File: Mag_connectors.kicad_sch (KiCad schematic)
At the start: 4 parts

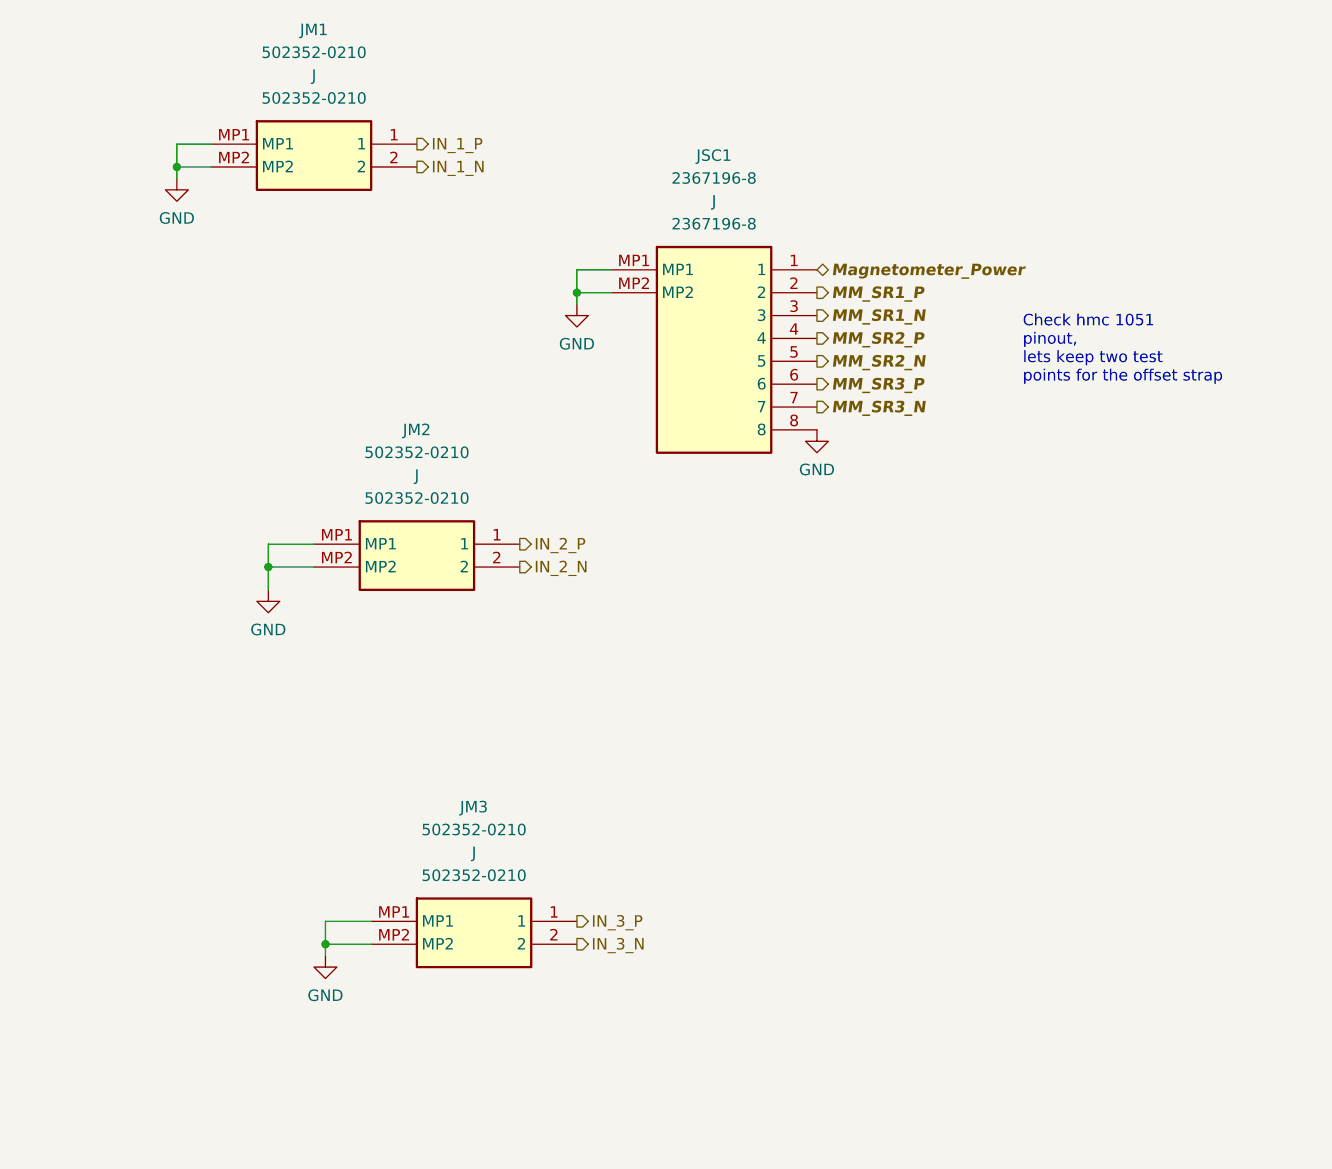
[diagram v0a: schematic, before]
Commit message: magnetometer connector corrected
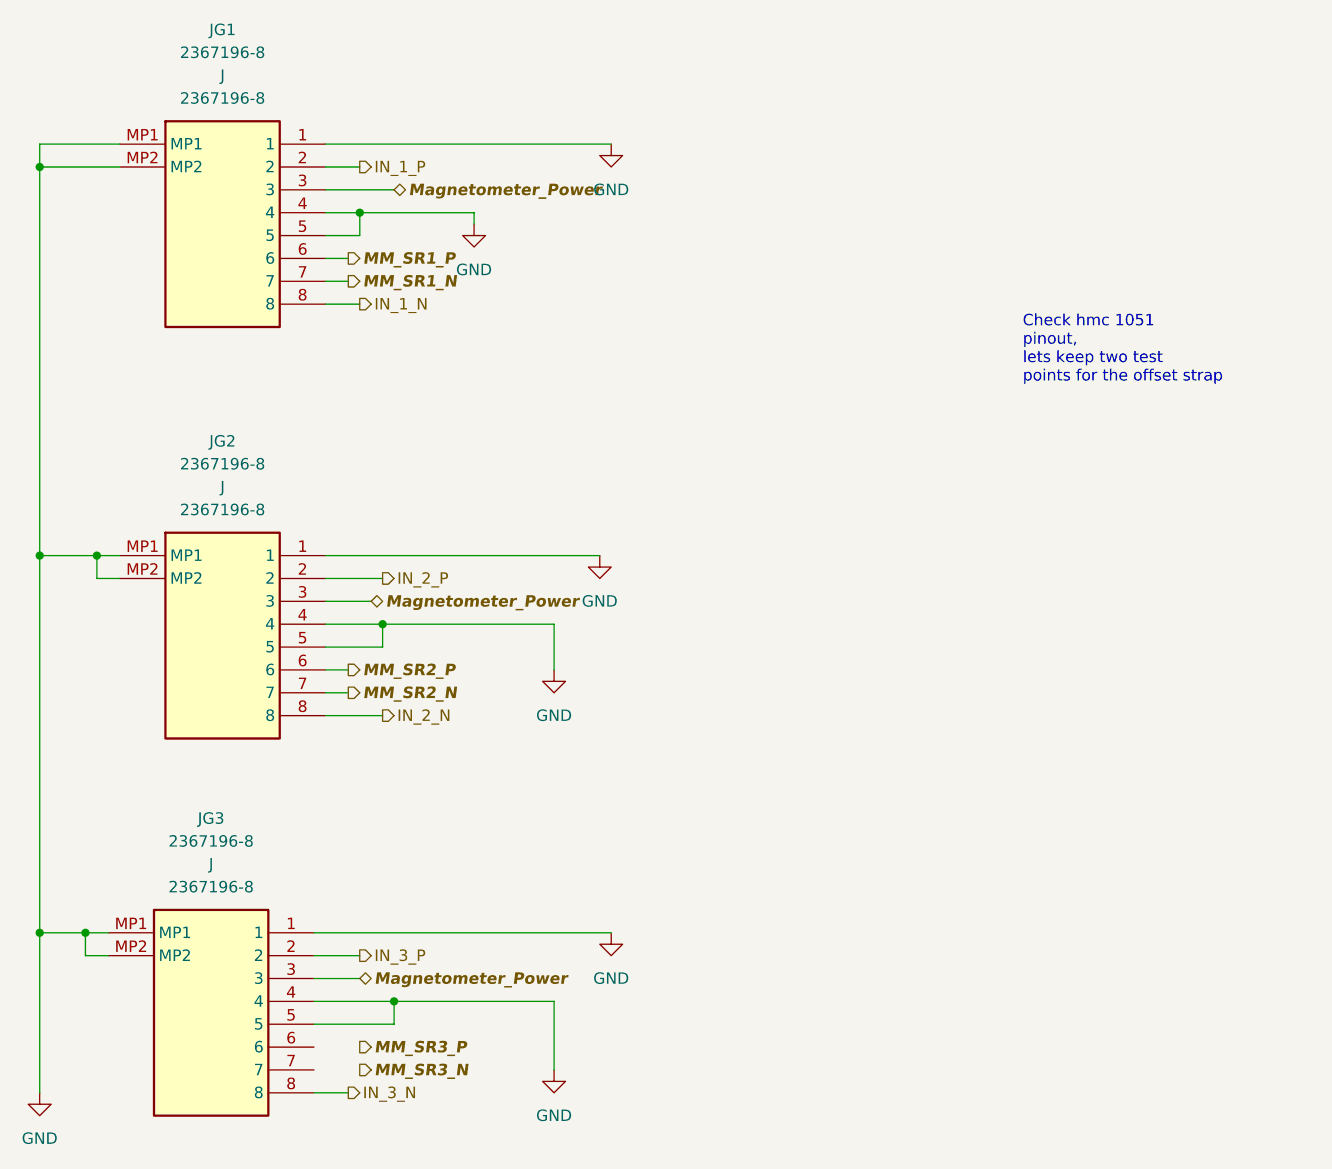
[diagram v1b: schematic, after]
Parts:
- removed JM1, JM2, JM3: 502352-0210, symbol 502352-0210:502352-0210
- removed JSC1: 2367196-8, symbol 2367196-8:2367196-8
- added JG1, JG2, JG3: 2367196-8, symbol 2367196-8:2367196-8
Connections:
- net GND: now also JG1.1, JG1.4, JG1.5, JG1.MP1, JG1.MP2, JG2.1, JG2.4, JG2.5, JG2.MP1, JG2.MP2, JG3.1, JG3.4, JG3.5, JG3.MP1, JG3.MP2
- net IN_1_N: now also JG1.8
- net IN_1_P: now also JG1.2
- net IN_2_N: now also JG2.8
- net IN_2_P: now also JG2.2
- net IN_3_N: now also JG3.8
- net IN_3_P: now also JG3.2
- net MM_SR1_N: now also JG1.7
- net MM_SR1_P: now also JG1.6
- net MM_SR2_N: now also JG2.7
- net MM_SR2_P: now also JG2.6
- net Magnetometer_Power: now also JG1.3, JG2.3, JG3.3

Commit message: ERC cleared in magnetometer connectors sheet
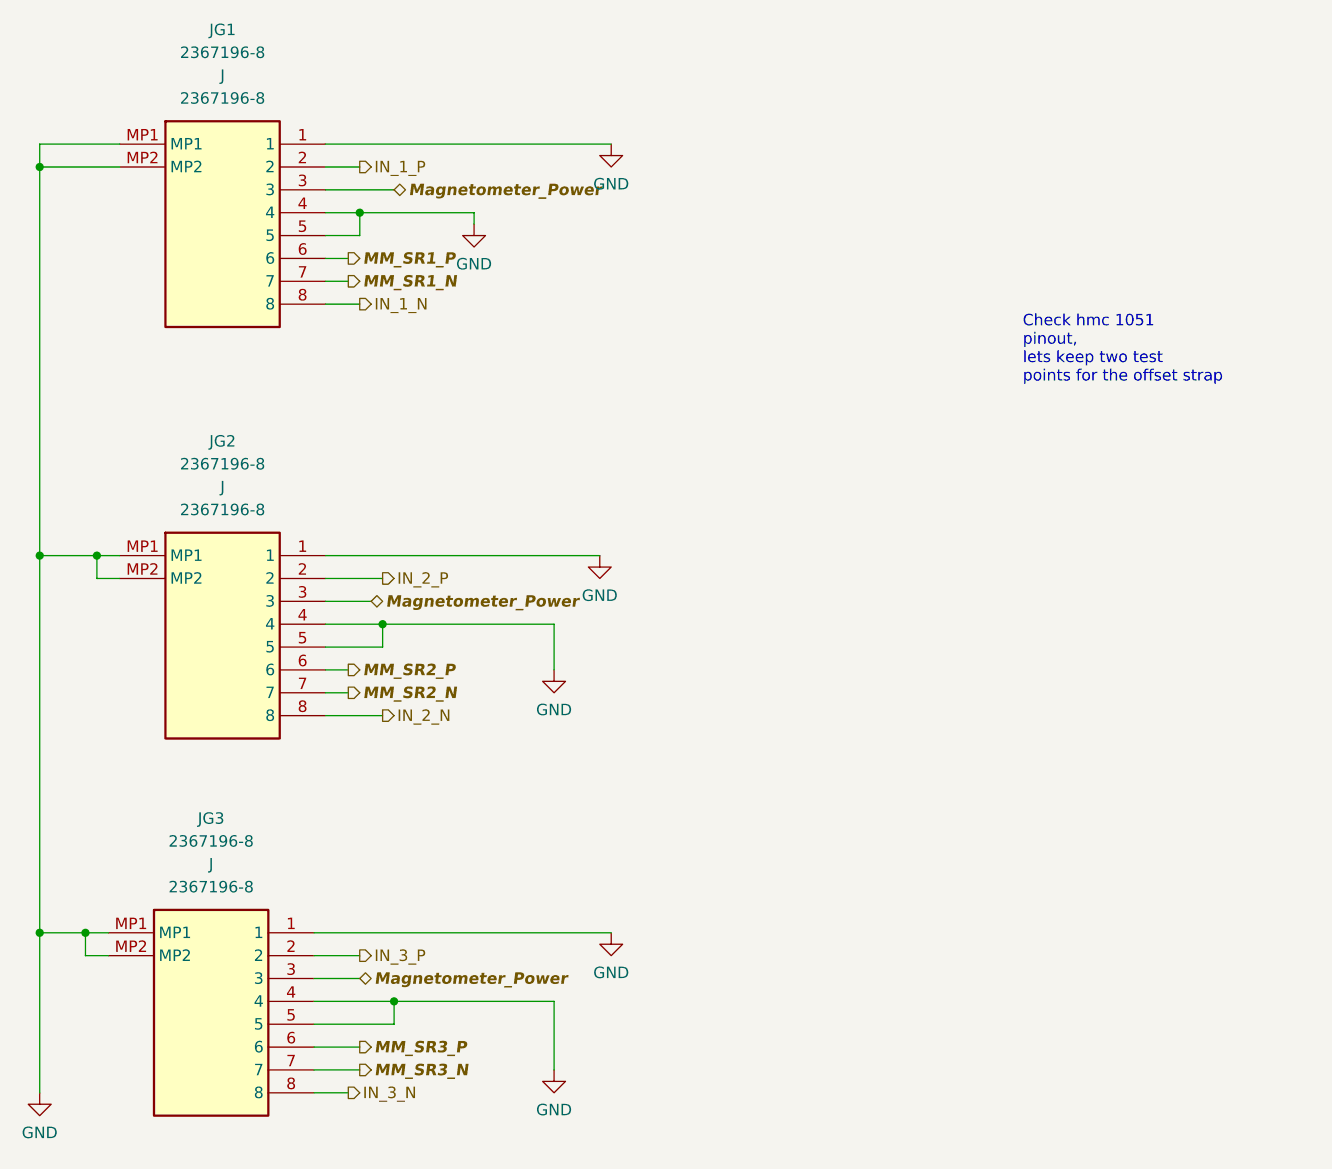
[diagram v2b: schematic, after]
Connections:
- net MM_SR3_N: now also JG3.7
- net MM_SR3_P: now also JG3.6
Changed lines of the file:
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@@
+    (stroke (width 0) (type default) (color 0 0 0 0))
+  )
+  (wire (pts (xy 76.2 149.86) (xy 81.28 149.86))
     (stroke (width 0) (type default) (color 0 0 0 0))
   )
   (wire (pts (xy 102.87 102.87) (xy 102.87 107.95))
+    (stroke (width 0) (type default) (color 0 0 0 0))
+  )
+  (wire (pts (xy 76.2 152.4) (xy 81.28 152.4))
     (stroke (width 0) (type default) (color 0 0 0 0))
   )
@@
   (hierarchical_label "Magnetometer_Power" (shape bidirectional) (at 82.55 100.33 0)
     (effects (font (size 1.27 1.27) bold italic) (justify left))
-  )
-  (symbol (lib_id "power:GND") (at 102.87 152.4 0) (unit 1)
-    (in_bom yes) (on_board yes) (fields_autoplaced)
-    (property "Reference" "#PWR?" (id 0) (at 102.87 158.75 0)
-      (effects (font (size 1.27 1.27)) hide)
-    )
-    (property "Value" "GND" (id 1) (at 102.87 157.48 0))
-    (property "Footprint" "" (id 2) (at 102.87 152.4 0)
-      (effects (font (size 1.27 1.27)) hide)
-    )
-    (property "Datasheet" "" (id 3) (at 102.87 152.4 0)
-      (effects (font (size 1.27 1.27)) hide)
-    )
-    (pin "1")
-  )
-  (symbol (lib_id "power:GND") (at 109.22 49.53 0) (unit 1)
-    (in_bom yes) (on_board yes) (fields_autoplaced)
-    (property "Reference" "#PWR?" (id 0) (at 109.22 55.88 0)
-      (effects (font (size 1.27 1.27)) hide)
-    )
-    (property "Value" "GND" (id 1) (at 109.22 54.61 0))
-    (property "Footprint" "" (id 2) (at 109.22 49.53 0)
-      (effects (font (size 1.27 1.27)) hide)
-    )
-    (property "Datasheet" "" (id 3) (at 109.22 49.53 0)
-      (effects (font (size 1.27 1.27)) hide)
-    )
-    (pin "1")
   )
   (symbol (lib_id "2367196-8:2367196-8") (at 54.61 95.25 0) (unit 1)
@@
     (pin "MP2")
   )
-  (symbol (lib_id "power:GND") (at 102.87 107.95 0) (unit 1)
-    (in_bom yes) (on_board yes) (fields_autoplaced)
-    (property "Reference" "#PWR?" (id 0) (at 102.87 114.3 0)
-      (effects (font (size 1.27 1.27)) hide)
-    )
-    (property "Value" "GND" (id 1) (at 102.87 113.03 0))
-    (property "Footprint" "" (id 2) (at 102.87 107.95 0)
-      (effects (font (size 1.27 1.27)) hide)
-    )
-    (property "Datasheet" "" (id 3) (at 102.87 107.95 0)
-      (effects (font (size 1.27 1.27)) hide)
-    )
+  (symbol (lib_id "upsat-comms-hardware:GND") (at 109.22 49.53 0) (unit 1)
+    (in_bom yes) (on_board yes) (fields_autoplaced)
+    (property "Reference" "#PWR0150" (id 0) (at 109.22 55.88 0)
+      (effects (font (size 1.27 1.27)) hide)
+    )
+    (property "Value" "GND" (id 1) (at 109.22 53.975 0))
+    (property "Footprint" "" (id 2) (at 109.22 49.53 0))
+    (property "Datasheet" "" (id 3) (at 109.22 49.53 0))
+    (pin "1")
+  )
+  (symbol (lib_id "upsat-comms-hardware:GND") (at 102.87 107.95 0) (unit 1)
+    (in_bom yes) (on_board yes) (fields_autoplaced)
+    (property "Reference" "#PWR0153" (id 0) (at 102.87 114.3 0)
+      (effects (font (size 1.27 1.27)) hide)
+    )
+    (property "Value" "GND" (id 1) (at 102.87 112.395 0))
+    (property "Footprint" "" (id 2) (at 102.87 107.95 0))
+    (property "Datasheet" "" (id 3) (at 102.87 107.95 0))
+    (pin "1")
+  )
+  (symbol (lib_id "upsat-comms-hardware:GND") (at 102.87 152.4 0) (unit 1)
+    (in_bom yes) (on_board yes) (fields_autoplaced)
+    (property "Reference" "#PWR0155" (id 0) (at 102.87 158.75 0)
+      (effects (font (size 1.27 1.27)) hide)
+    )
+    (property "Value" "GND" (id 1) (at 102.87 156.845 0))
+    (property "Footprint" "" (id 2) (at 102.87 152.4 0))
+    (property "Datasheet" "" (id 3) (at 102.87 152.4 0))
+    (pin "1")
+  )
+  (symbol (lib_id "upsat-comms-hardware:GND") (at 45.72 154.94 0) (unit 1)
+    (in_bom yes) (on_board yes) (fields_autoplaced)
+    (property "Reference" "#PWR0156" (id 0) (at 45.72 161.29 0)
+      (effects (font (size 1.27 1.27)) hide)
+    )
+    (property "Value" "GND" (id 1) (at 45.72 159.385 0))
+    (property "Footprint" "" (id 2) (at 45.72 154.94 0))
+    (property "Datasheet" "" (id 3) (at 45.72 154.94 0))
     (pin "1")
   )
@@
     (pin "MP2")
   )
-  (symbol (lib_id "power:GND") (at 107.95 95.25 0) (unit 1)
-    (in_bom yes) (on_board yes) (fields_autoplaced)
-    (property "Reference" "#PWR?" (id 0) (at 107.95 101.6 0)
-      (effects (font (size 1.27 1.27)) hide)
-    )
-    (property "Value" "GND" (id 1) (at 107.95 100.33 0))
-    (property "Footprint" "" (id 2) (at 107.95 95.25 0)
-      (effects (font (size 1.27 1.27)) hide)
-    )
-    (property "Datasheet" "" (id 3) (at 107.95 95.25 0)
-      (effects (font (size 1.27 1.27)) hide)
-    )
-    (pin "1")
-  )
-  (symbol (lib_id "power:GND") (at 109.22 137.16 0) (unit 1)
-    (in_bom yes) (on_board yes) (fields_autoplaced)
-    (property "Reference" "#PWR?" (id 0) (at 109.22 143.51 0)
-      (effects (font (size 1.27 1.27)) hide)
-    )
-    (property "Value" "GND" (id 1) (at 109.22 142.24 0))
-    (property "Footprint" "" (id 2) (at 109.22 137.16 0)
-      (effects (font (size 1.27 1.27)) hide)
-    )
-    (property "Datasheet" "" (id 3) (at 109.22 137.16 0)
-      (effects (font (size 1.27 1.27)) hide)
-    )
-    (pin "1")
-  )
-  (symbol (lib_id "power:GND") (at 93.98 58.42 0) (unit 1)
-    (in_bom yes) (on_board yes) (fields_autoplaced)
-    (property "Reference" "#PWR?" (id 0) (at 93.98 64.77 0)
-      (effects (font (size 1.27 1.27)) hide)
-    )
-    (property "Value" "GND" (id 1) (at 93.98 63.5 0))
-    (property "Footprint" "" (id 2) (at 93.98 58.42 0)
-      (effects (font (size 1.27 1.27)) hide)
-    )
-    (property "Datasheet" "" (id 3) (at 93.98 58.42 0)
-      (effects (font (size 1.27 1.27)) hide)
-    )
-    (pin "1")
-  )
-  (symbol (lib_id "power:GND") (at 45.72 154.94 0) (unit 1)
-    (in_bom yes) (on_board yes) (fields_autoplaced)
-    (property "Reference" "#PWR?" (id 0) (at 45.72 161.29 0)
-      (effects (font (size 1.27 1.27)) hide)
-    )
-    (property "Value" "GND" (id 1) (at 45.72 160.02 0))
-    (property "Footprint" "" (id 2) (at 45.72 154.94 0)
-      (effects (font (size 1.27 1.27)) hide)
-    )
-    (property "Datasheet" "" (id 3) (at 45.72 154.94 0)
-      (effects (font (size 1.27 1.27)) hide)
-    )
-    (pin "1")
-  )
+  (symbol (lib_id "upsat-comms-hardware:GND") (at 107.95 95.25 0) (unit 1)
+    (in_bom yes) (on_board yes) (fields_autoplaced)
+    (property "Reference" "#PWR0152" (id 0) (at 107.95 101.6 0)
+      (effects (font (size 1.27 1.27)) hide)
+    )
+    (property "Value" "GND" (id 1) (at 107.95 99.695 0))
+    (property "Footprint" "" (id 2) (at 107.95 95.25 0))
+    (property "Datasheet" "" (id 3) (at 107.95 95.25 0))
+    (pin "1")
+  )
+  (symbol (lib_id "upsat-comms-hardware:GND") (at 93.98 58.42 0) (unit 1)
+    (in_bom yes) (on_board yes) (fields_autoplaced)
+    (property "Reference" "#PWR0151" (id 0) (at 93.98 64.77 0)
+      (effects (font (size 1.27 1.27)) hide)
+    )
+    (property "Value" "GND" (id 1) (at 93.98 62.865 0))
+    (property "Footprint" "" (id 2) (at 93.98 58.42 0))
+    (property "Datasheet" "" (id 3) (at 93.98 58.42 0))
+    (pin "1")
+  )
+  (symbol (lib_id "upsat-comms-hardware:GND") (at 109.22 137.16 0) (unit 1)
+    (in_bom yes) (on_board yes) (fields_autoplaced)
+    (property "Reference" "#PWR0154" (id 0) (at 109.22 143.51 0)
+      (effects (font (size 1.27 1.27)) hide)
+    )
+    (property "Value" "GND" (id 1) (at 109.22 141.605 0))
+    (property "Footprint" "" (id 2) (at 109.22 137.16 0))
+    (property "Datasheet" "" (id 3) (at 109.22 137.16 0))
+    (pin "1")
+  )
